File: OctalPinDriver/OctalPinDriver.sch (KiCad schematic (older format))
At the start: 1 part

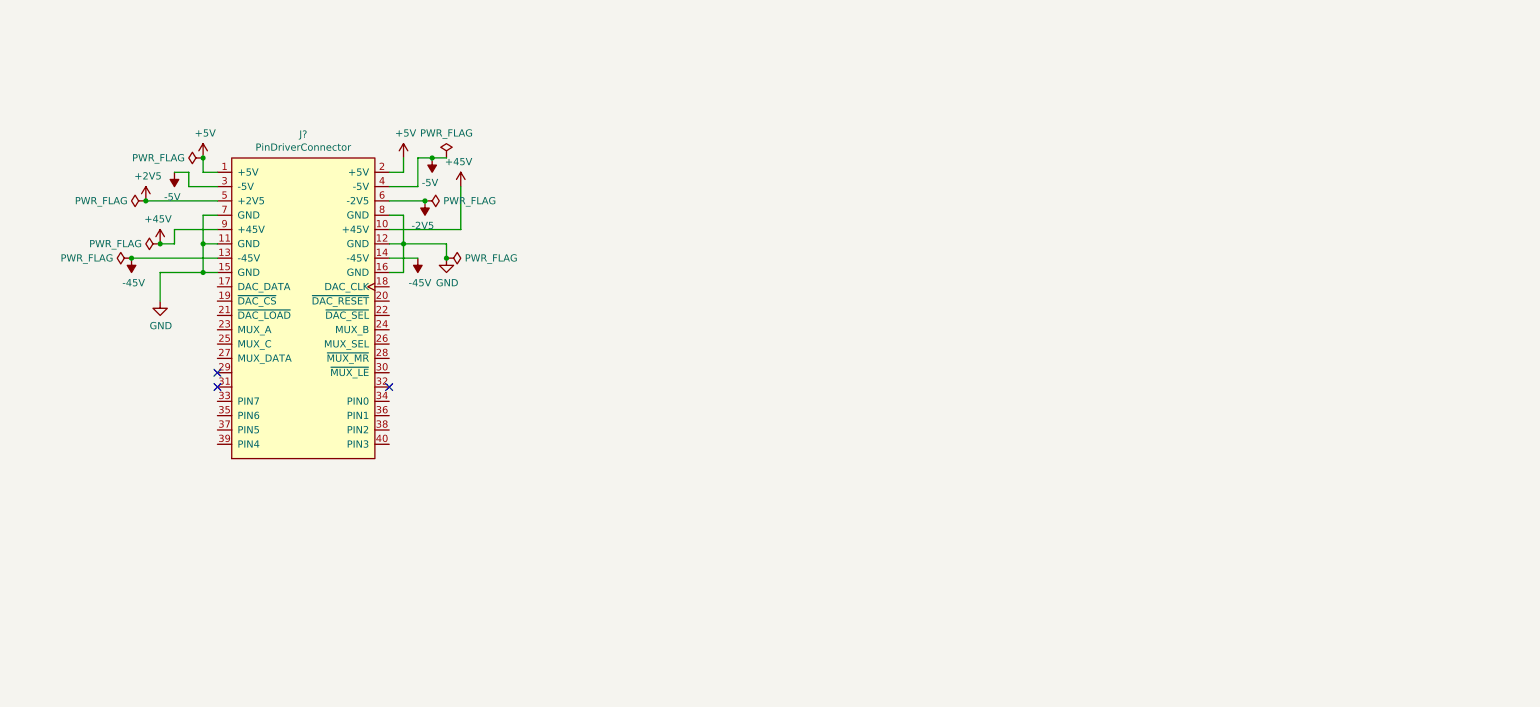
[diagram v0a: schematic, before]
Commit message: more work on pin driver
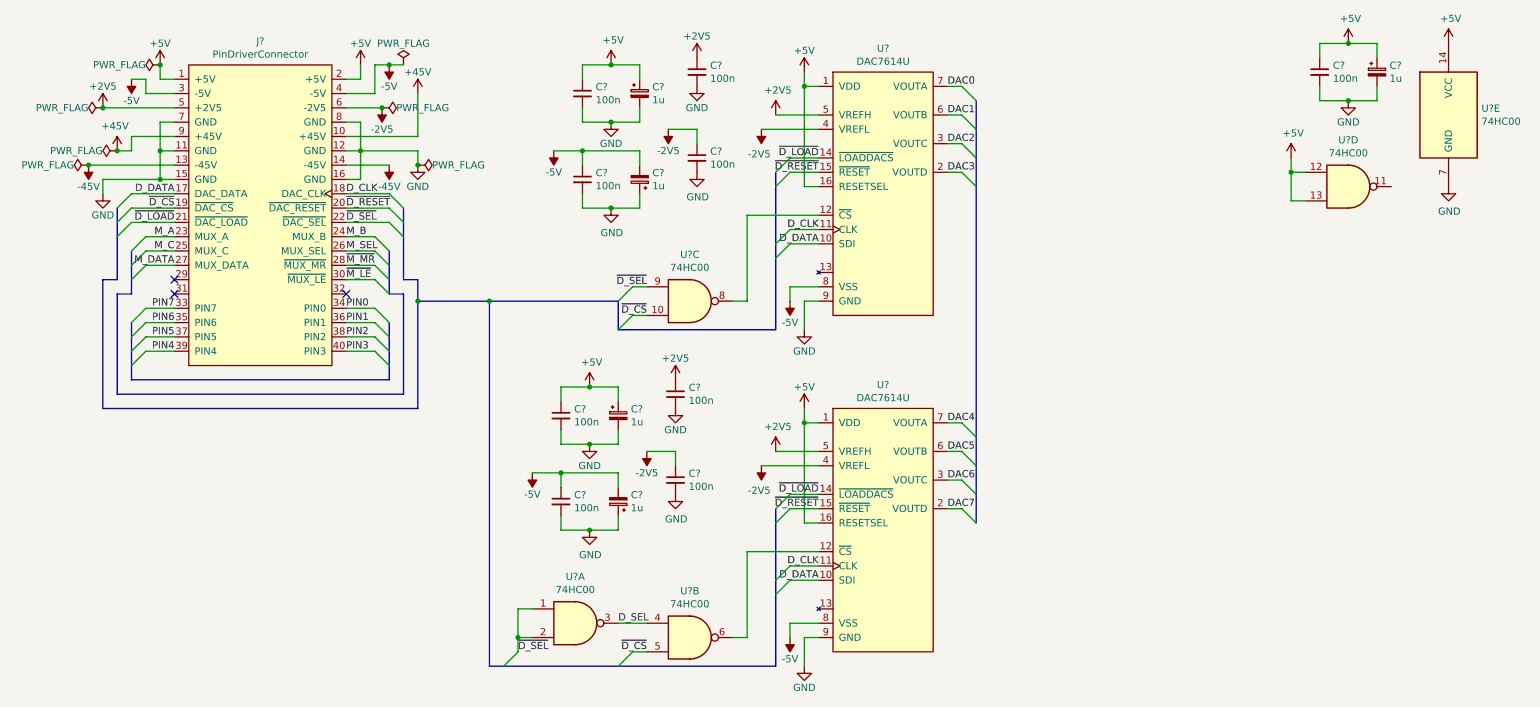
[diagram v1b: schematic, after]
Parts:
- added C? (x5): 1u, symbol Device:CP_Small
- added C? (x9): 100n, symbol Device:C_Small
- added U? (x2): DAC7614U, Package_SO:SOIC-16W_7.5x10.3mm_P1.27mm, symbol UniProg:DAC7614U
- added U? (x5): 74HC00, symbol 74xx:74HC00
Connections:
- net +2V5: now also C?.1, C?.1, U?.5 (VREFH), U?.5 (VREFH)
- net +5V: now also C?.1, C?.1, C?.1, C?.1, C?.1, C?.1, U?.1 (VDD), U?.1 (VDD), U?.12, U?.13, U?.14 (VCC), U?.16 (RESETSEL), U?.16 (RESETSEL)
- net -2V5: now also C?.1, C?.1, U?.4 (VREFL), U?.4 (VREFL)
- net -5V: now also C?.1, C?.1, C?.2, C?.2, U?.8 (VSS), U?.8 (VSS)
- net GND: now also C?.1, C?.1, C?.2, C?.2, C?.2, C?.2, C?.2, C?.2, C?.2, C?.2, C?.2, C?.2, C?.2, C?.2, U?.7 (GND), U?.9 (GND), U?.9 (GND)
- net D_DATA: now reaches J?.17 (DAC_DATA)
- net D_DATA: now also U?.10 (SDI), U?.10 (SDI)
- net D_CLK: now reaches J?.18 (DAC_CLK)
- net D_CLK: now also U?.11 (CLK), U?.11 (CLK)
- net ~D_CS: now reaches J?.19 (~DAC_CS)
- net ~D_CS: now also U?.10, U?.5
- net ~D_RESET: now reaches J?.20 (~DAC_RESET)
- net ~D_RESET: now also U?.15 (~RESET), U?.15 (~RESET)
- net ~D_LOAD: now reaches J?.21 (~DAC_LOAD)
- net ~D_LOAD: now also U?.14 (~LOADDACS), U?.14 (~LOADDACS)
- net ~D_SEL: now reaches J?.22 (~DAC_SEL)
- net ~D_SEL: now also U?.1, U?.2, U?.9
- net M_A: now reaches J?.23 (MUX_A)
- net M_B: now reaches J?.24 (MUX_B)
- net M_C: now reaches J?.25 (MUX_C)
- net M_SEL: now reaches J?.26 (MUX_SEL)
- net M_DATA: now reaches J?.27 (MUX_DATA)
- net ~M_MR: now reaches J?.28 (~MUX_MR)
- net ~M_LE: now reaches J?.30 (~MUX_LE)
- net PIN7: now reaches J?.33 (PIN7)
- net PIN0: now reaches J?.34 (PIN0)
- net PIN6: now reaches J?.35 (PIN6)
- net PIN1: now reaches J?.36 (PIN1)
- net PIN5: now reaches J?.37 (PIN5)
- net PIN2: now reaches J?.38 (PIN2)
- net PIN4: now reaches J?.39 (PIN4)
- net PIN3: now reaches J?.40 (PIN3)
- new net: U?.12 (~CS), U?.8
- new net: U?.12 (~CS), U?.6
- new net DAC0: U?.7 (VOUTA)
- new net DAC1: U?.6 (VOUTB)
- new net DAC2: U?.3 (VOUTC)
- new net DAC3: U?.2 (VOUTD)
- new net DAC4: U?.7 (VOUTA)
- new net DAC5: U?.6 (VOUTB)
- new net DAC6: U?.3 (VOUTC)
- new net DAC7: U?.2 (VOUTD)
- new net D_SEL: U?.3, U?.4
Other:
- moved on the sheet: J?
